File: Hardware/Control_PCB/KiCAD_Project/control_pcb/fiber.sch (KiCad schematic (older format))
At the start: 6 parts, among them U4 IF-D96F, U5 TC4S584F

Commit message: Control PCB Rev 1.0 complete.
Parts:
- added Q1: BSS138, TO_SOT_Packages_SMD:SOT-23, symbol Transistor_FET:BSS138
- added R27, R28: 10k, Resistors_SMD:R_0603_HandSoldering, symbol Device:R
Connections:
- net +BATT: now also R27.1
- net Fiber_Serial_In: now also Q1.2 (S), R28.2; no longer R18.1, R19.1
- new net: Q1.3 (D), R18.1, R19.1, R27.2
- new net +3V3: Q1.1 (G), R28.1
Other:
- moved on the sheet: C12, C13, R18, R19, U4, U5

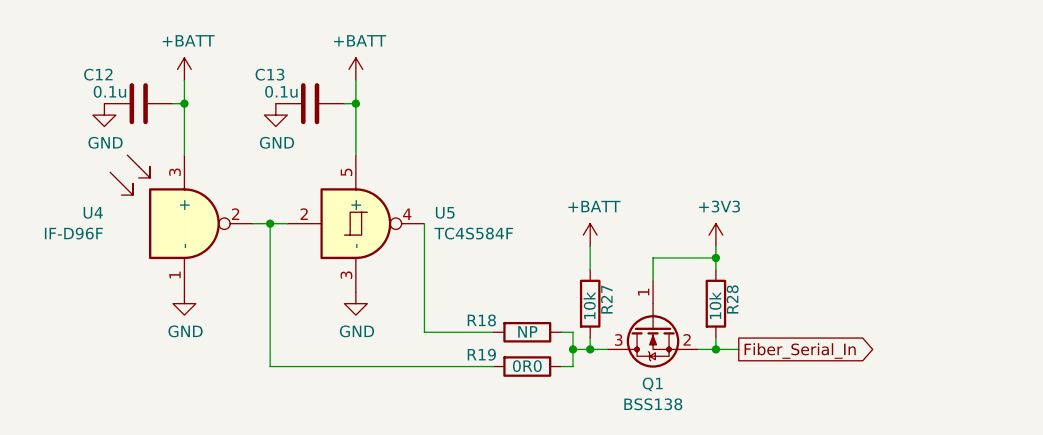
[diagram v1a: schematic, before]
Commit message: Add pullup to fiber optic receiver. Closes #12.
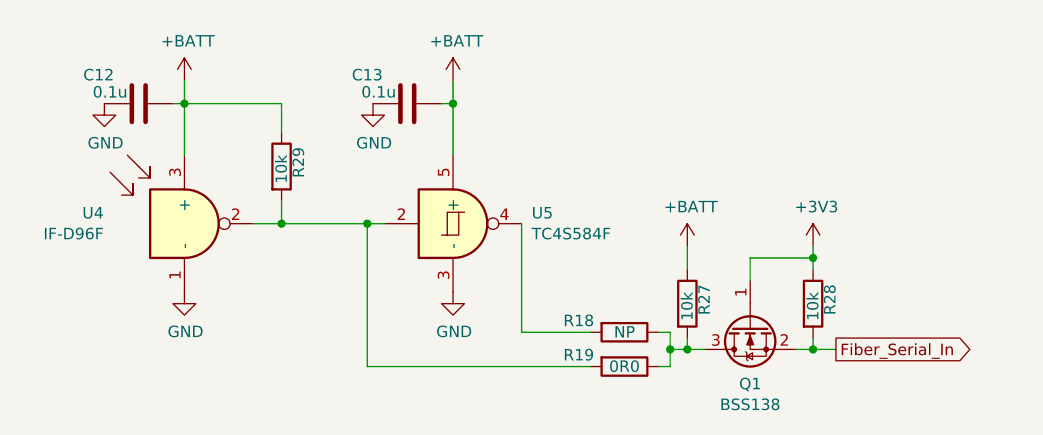
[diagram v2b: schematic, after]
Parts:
- added R29: 10k, Resistor_SMD:R_0603_1608Metric_Pad1.05x0.95mm_HandSolder, symbol Device:R
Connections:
- net +BATT: now also R29.1
- net at R19.2, U4.2, U5.2: now also R29.2
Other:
- moved on the sheet: C13, Q1, R18, R19, R27, R28, U5
